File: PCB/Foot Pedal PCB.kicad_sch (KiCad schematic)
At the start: 10 parts, among them J1 Conn_01x03_Female, SW1 SW_Push, SW2 SW_Push, SW3 SW_Push, U1 ProMicro

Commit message: PCB changes and incremental readme writes
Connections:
- net ROW0: now reaches C1.2, J1.2 (Pin_2), SW2.2, SW3.2, U1.12 (B5)
- net COL2: now reaches J1.3 (Pin_3), U1.13 (B6)
- net COL1: now reaches SW3.1, U1.14 (B2)
- net COL0: now reaches SW2.1, U1.15 (B3)
- net LED2: now reaches D2.1 (K), U1.19 (F5)
- net LED1: now reaches D1.1 (K), U1.20 (F4)
- net VCC: now reaches R1.1, R2.1, U1.21 (VCC)
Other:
- moved on the sheet: C1, D1, D2, J1, R1, R2, SW1, SW2, SW3, U1

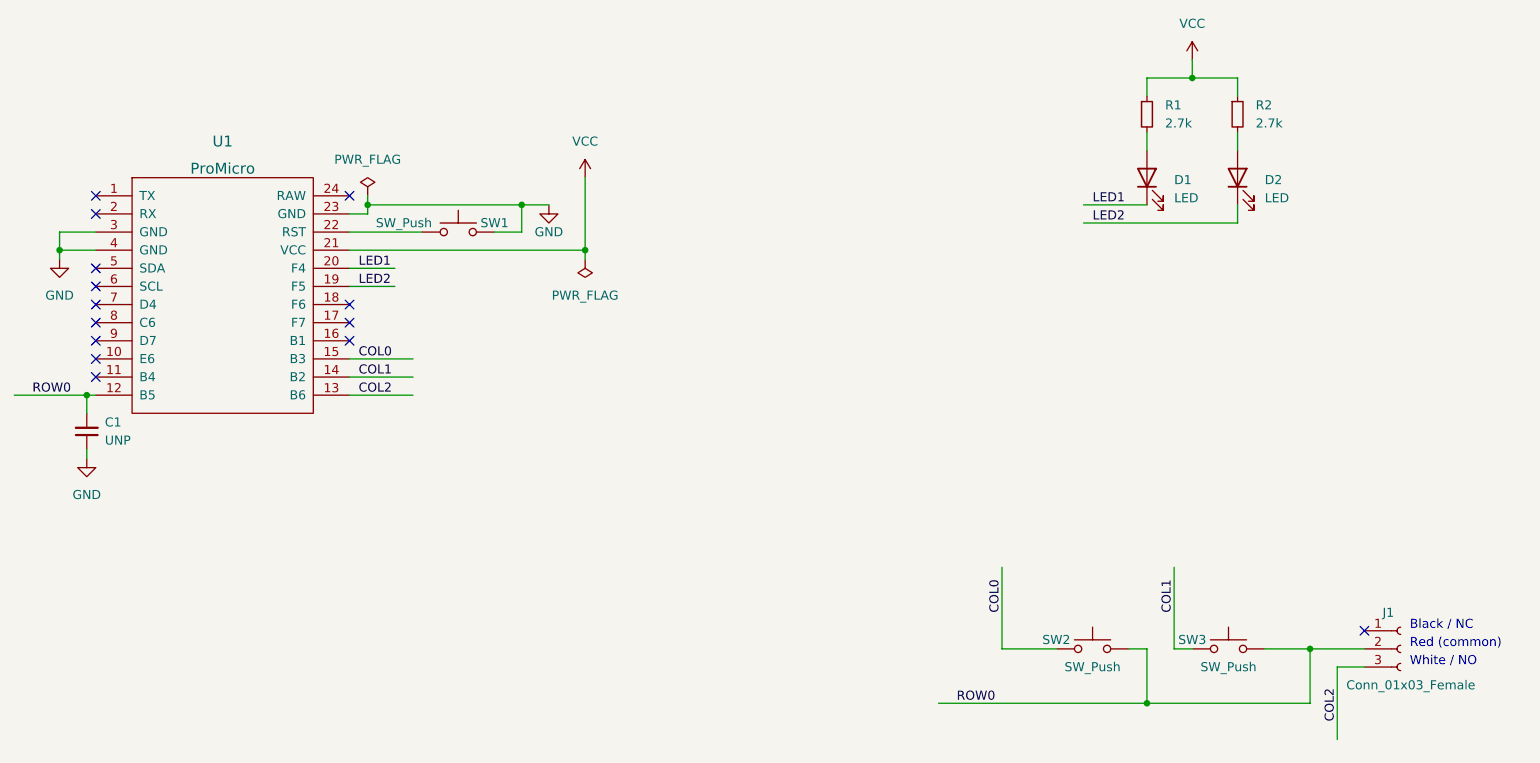
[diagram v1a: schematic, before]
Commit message: Added PDF and SVG plots of the schematic and PCB layers.  Added revision B which has direct pull-down on all keys.
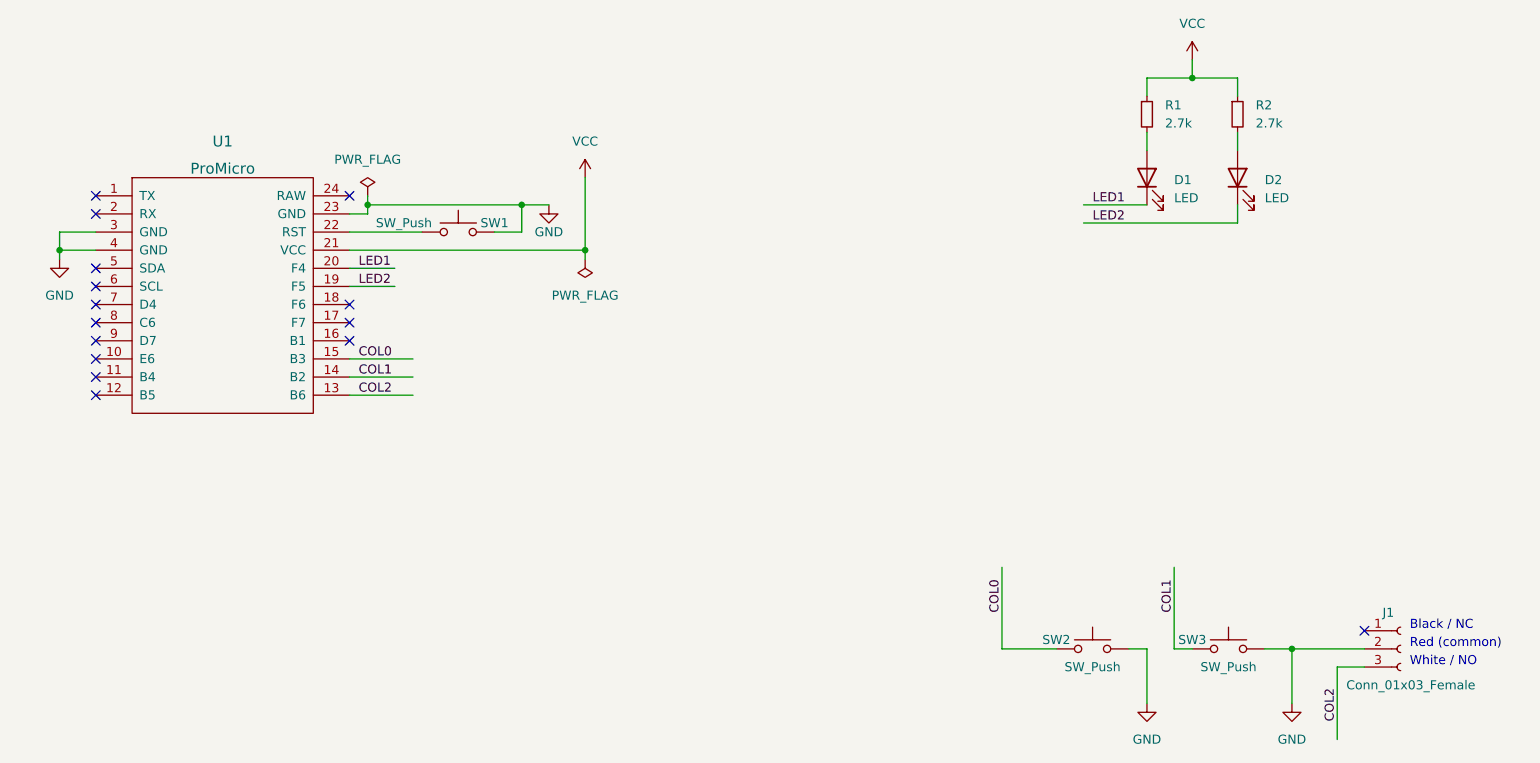
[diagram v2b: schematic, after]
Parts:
- removed C1: UNP, Capacitor_SMD:C_0805_2012Metric, symbol Device:C_Small
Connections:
- net GND: now also J1.2 (Pin_2), SW2.2, SW3.2
- removed net ROW0: J1.2 (Pin_2), SW2.2, SW3.2, U1.12 (B5)
- no-connect marks 14 -> 15
